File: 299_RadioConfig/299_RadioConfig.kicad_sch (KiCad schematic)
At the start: 13 parts, among them SW1 Bourns PEC11R, SW2 SW_Push_Dual, U1 RPi_Pico_TH, U2 RDA5807M_Module, U3 LM386

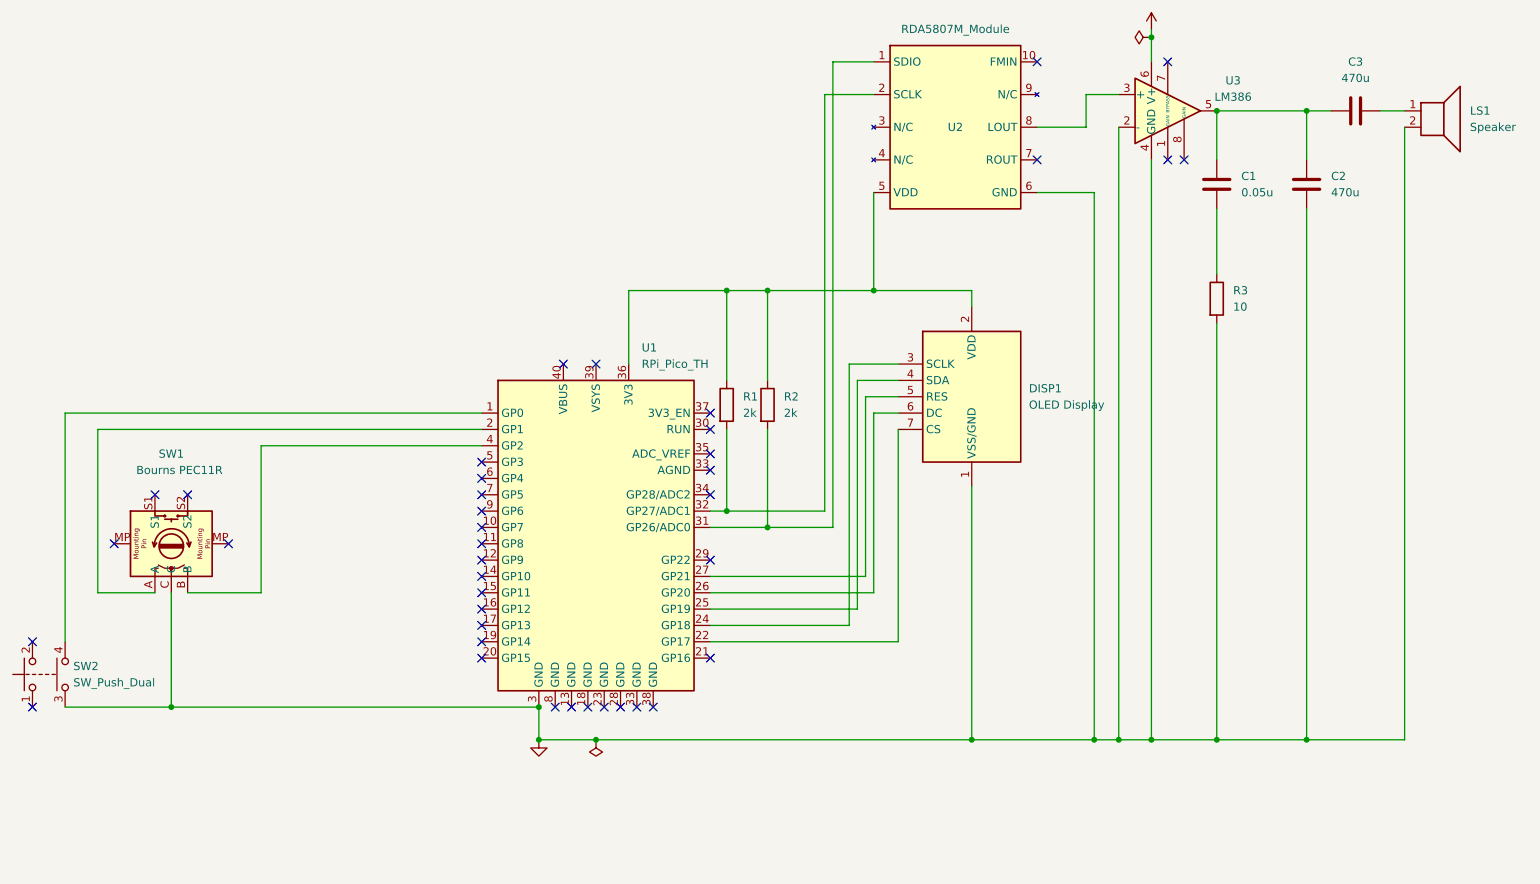
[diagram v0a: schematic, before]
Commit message: Updated Radio Config, as ordered from JLCPCB
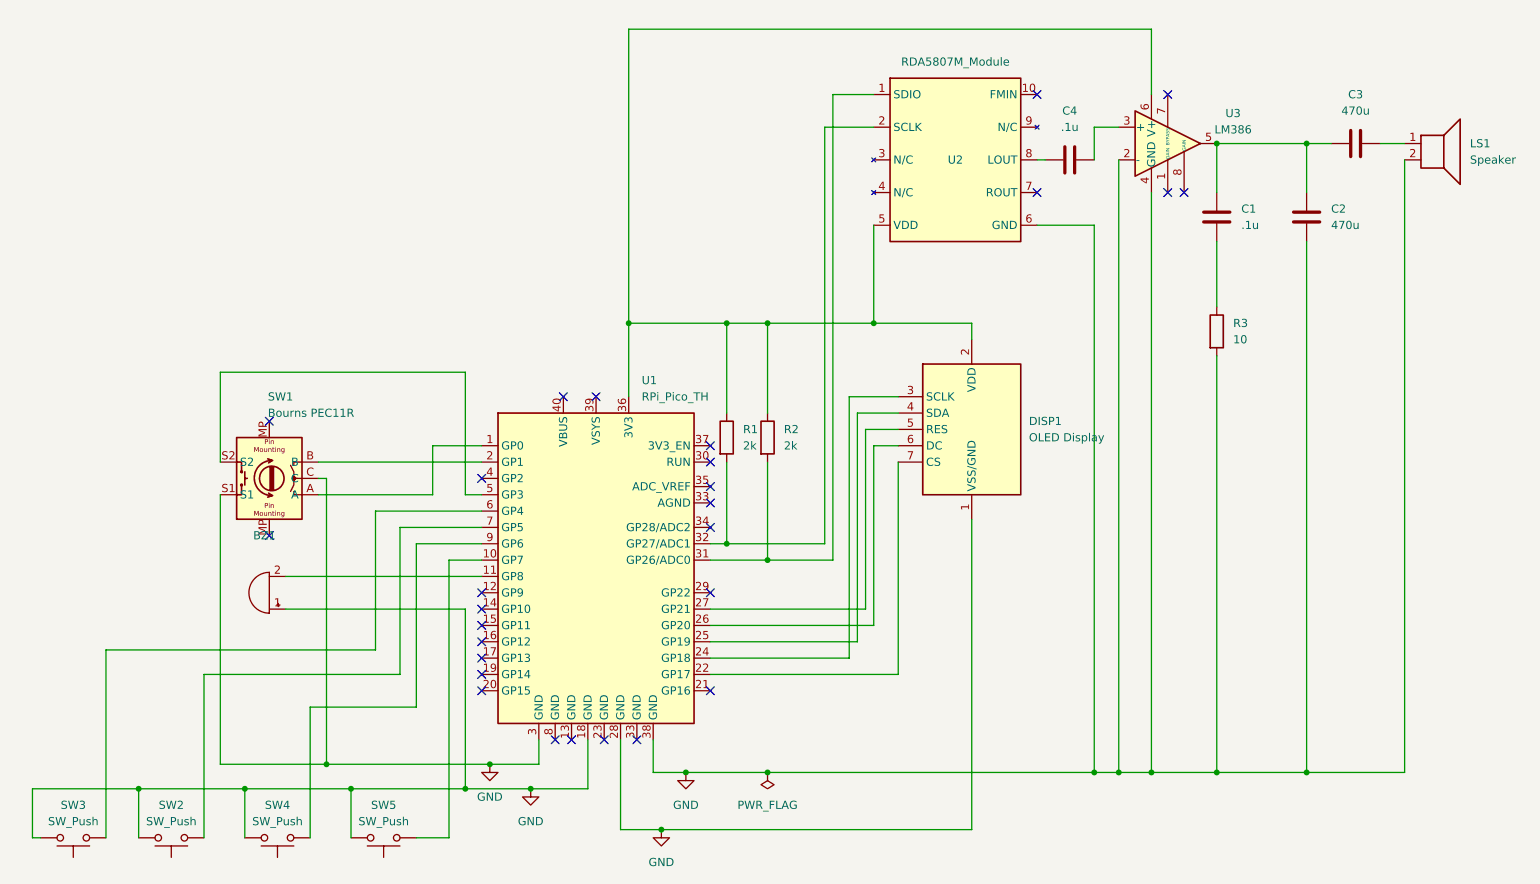
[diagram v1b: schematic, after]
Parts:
- removed SW2: SW_Push_Dual, symbol Switch:SW_Push_Dual
- added BZ1: (no value), symbol Device:Buzzer
- added C4: .1u, Capacitor_THT:C_Axial_L3.8mm_D2.6mm_P7.50mm_Horizontal, symbol Device:C
- added SW2, SW3, SW4, SW5: SW_Push, Connector_PinHeader_2.54mm:PinHeader_1x02_P2.54mm_Vertical, symbol Switch:SW_Push
- C1: value 0.05u -> .1u; footprint (none) -> Capacitor_THT:C_Axial_L3.8mm_D2.6mm_P7.50mm_Horizontal
- C2: footprint (none) -> Capacitor_THT:C_Radial_D6.3mm_H11.0mm_P2.50mm
- C3: footprint (none) -> Capacitor_THT:C_Radial_D5.0mm_H11.0mm_P2.00mm
- DISP1: footprint ECE:OLED_Display_1.3 -> Connector_PinHeader_2.54mm:PinHeader_1x07_P2.54mm_Vertical
- LS1: footprint (none) -> TerminalBlock_Phoenix:TerminalBlock_Phoenix_MKDS-1,5-2_1x02_P5.00mm_Horizontal
- R1, R2, R3: footprint (none) -> Resistor_THT:R_Axial_DIN0207_L6.3mm_D2.5mm_P10.16mm_Horizontal
- SW1: footprint Rotary_Encoder:RotaryEncoder_Alps_EC12E-Switch_Vertical_H20mm -> Rotary_Encoder:RotaryEncoder_Alps_EC12E-Switch_Vertical_H20mm_CircularMountingHoles
- U3: footprint (none) -> Package_DIP:DIP-8_W7.62mm
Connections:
- net VCC is gone; now on an unnamed net: U3.6 (V+)
- net GND: now also SW1.S1, U1.18 (GND), U1.28 (GND), U1.38 (GND), BZ1.1 (-), SW2.2, SW3.2, SW4.2, SW5.2
- net at U1.1 (GP0): now also SW1.A
- net at U1.10 (GP7): now also SW5.1
- net at U1.11 (GP8): now also BZ1.2 (+)
- net at U1.2 (GP1): now also SW1.B; no longer SW1.A
- net at U1.4 (GP2): no longer SW1.B
- net at U1.5 (GP3): now also SW1.S2
- net at U1.6 (GP4): now also SW3.1
- net at U1.7 (GP5): now also SW2.1
- net at U1.9 (GP6): now also SW4.1
- net at U3.3 (+): now also C4.2; no longer U2.8 (LOUT)
- new net: C4.1, U2.8 (LOUT)
- no-connect marks 40 -> 28
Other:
- moved on the sheet: C1, C2, C3, DISP1, LS1, R1, R2, R3, U1, U2, U3
